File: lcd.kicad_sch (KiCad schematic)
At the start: 6 parts, among them J2 LCD 3.2" 240x320 Conn_01x14_P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

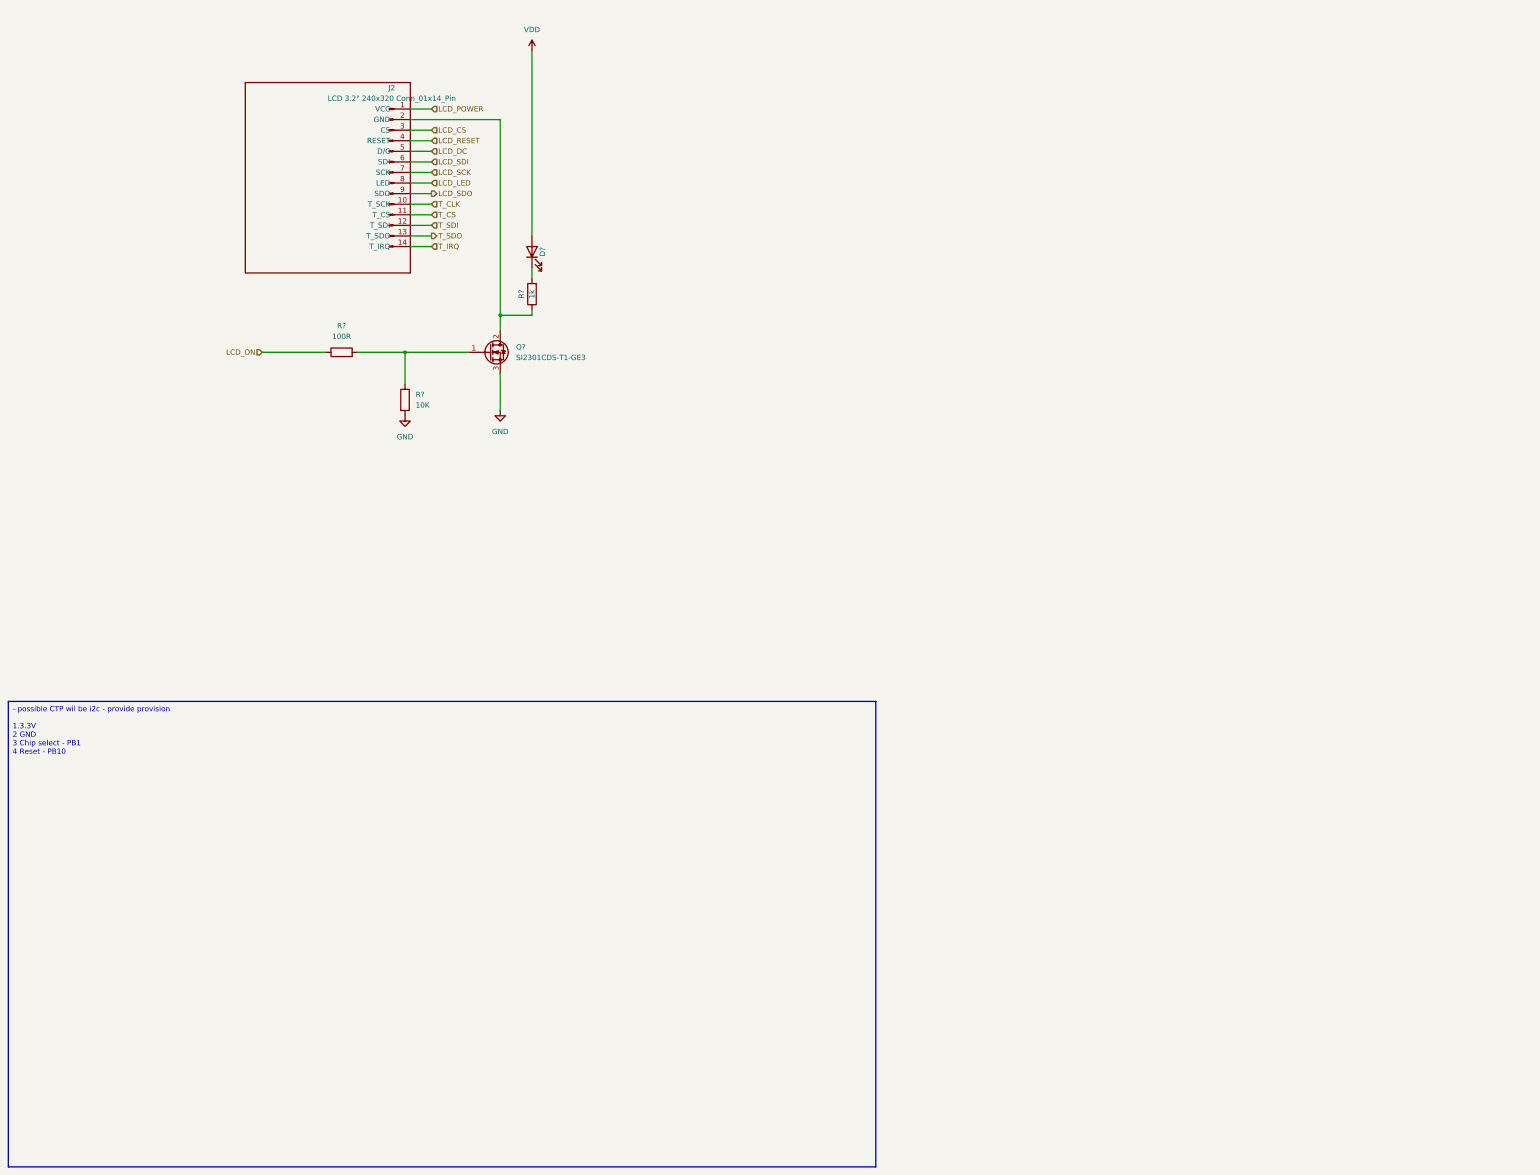
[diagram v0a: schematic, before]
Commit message: change power add buzzer
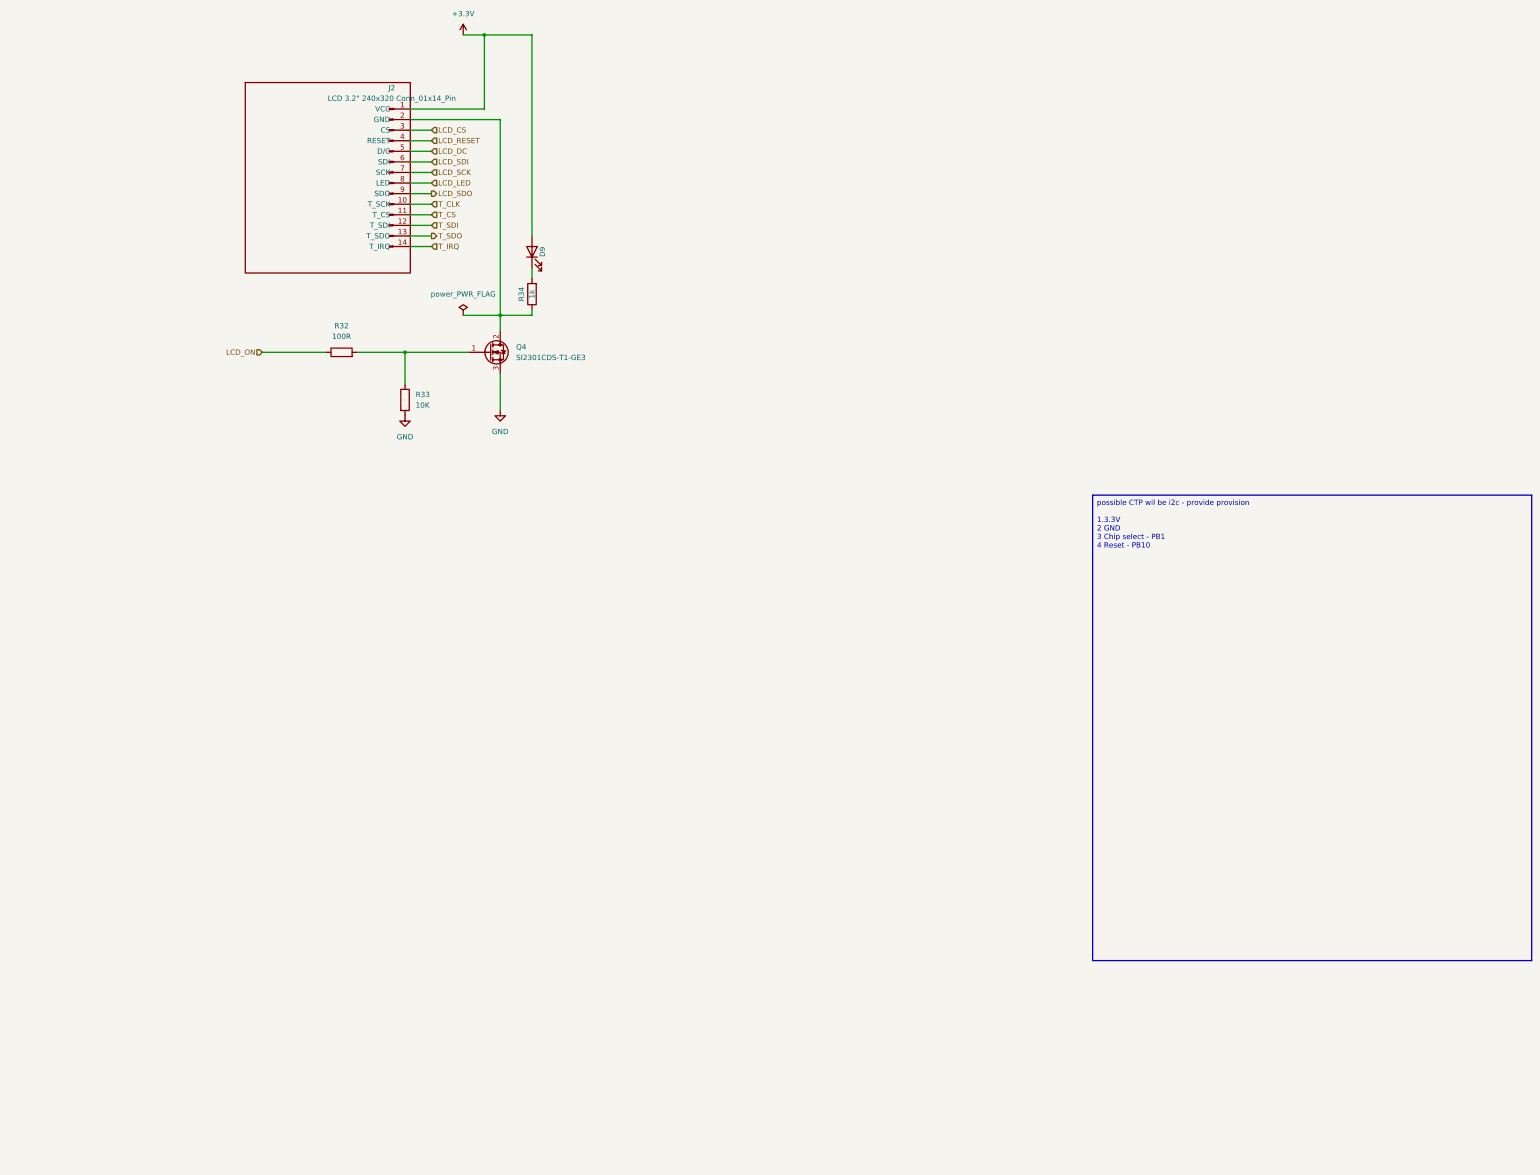
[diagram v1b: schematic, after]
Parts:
- gave numbers to parts that had none: 5
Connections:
- net VDD is gone; now on net +3.3V: D9.2 (A)
- net LCD_POWER renamed +3.3V
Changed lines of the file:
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@@
+	)
+	(junction
+		(at 153.67 27.94)
+		(diameter 0)
+		(color 0 0 0 0)
 	)
 	(junction
@@
 	(wire
 		(pts
-			(xy 135.89 45.72) (xy 140.97 45.72)
+			(xy 135.89 45.72) (xy 153.67 45.72)
 		)
 		(stroke
@@
 	(wire
 		(pts
+			(xy 148.59 95.25) (xy 157.48 95.25)
+		)
+		(stroke
+			(width 0)
+			(type default)
+		)
+	)
+	(wire
+		(pts
 			(xy 123.19 104.14) (xy 134.62 104.14)
 		)
@@
 	(wire
 		(pts
+			(xy 165.1 27.94) (xy 165.1 76.2)
+		)
+		(stroke
+			(width 0)
+			(type default)
+		)
+	)
+	(wire
+		(pts
+			(xy 153.67 27.94) (xy 153.67 45.72)
+		)
+		(stroke
+			(width 0)
+			(type default)
+		)
+	)
+	(wire
+		(pts
 			(xy 135.89 63.5) (xy 140.97 63.5)
 		)
@@
 	(wire
 		(pts
+			(xy 153.67 27.94) (xy 165.1 27.94)
+		)
+		(stroke
+			(width 0)
+			(type default)
+		)
+	)
+	(wire
+		(pts
 			(xy 135.89 53.34) (xy 140.97 53.34)
 		)
@@
 	(wire
 		(pts
+			(xy 148.59 27.94) (xy 153.67 27.94)
+		)
+		(stroke
+			(width 0)
+			(type default)
+		)
+	)
+	(wire
+		(pts
 			(xy 165.1 83.82) (xy 165.1 86.36)
 		)
@@
 	(wire
 		(pts
-			(xy 165.1 31.75) (xy 165.1 76.2)
-		)
-		(stroke
-			(width 0)
-			(type default)
-		)
-	)
-	(wire
-		(pts
 			(xy 100.33 104.14) (xy 115.57 104.14)
 		)
@@
 		)
 	)
-	(text_box "- possible CTP wil be i2c - provide provision\n\n1.3.3V\n2 GND \n3 Chip select - PB1\n4 Reset - PB10\n"
+	(text_box "possible CTP wil be i2c - provide provision\n\n1.3.3V\n2 GND \n3 Chip select - PB1\n4 Reset - PB10\n"
 		(exclude_from_sim no)
-		(at 39.37 187.96 0)
-		(size 208.28 111.76)
+		(at 299.72 138.43 0)
+		(size 105.41 111.76)
 		(stroke
 			(width 0)
@@
 		)
 	)
-	(hierarchical_label "LCD_POWER"
-		(shape input)
-		(at 140.97 45.72 0)
-		(fields_autoplaced yes)
-		(effects
-			(font
-				(size 1.27 1.27)
-			)
-			(justify left)
-		)
-	)
 	(hierarchical_label "LCD_SCK"
 		(shape input)
@@
 			)
 			(justify left)
+		)
+	)
+	(symbol
+		(lib_id "power:+3.3V")
+		(at 148.59 27.94 0)
+		(unit 1)
+		(exclude_from_sim no)
+		(in_bom yes)
+		(on_board yes)
+		(dnp no)
+		(fields_autoplaced yes)
+		(property "Reference" "#PWR034"
+			(at 148.59 31.75 0)
+			(effects
+				(font
+					(size 1.27 1.27)
+				)
+				(hide yes)
+			)
+		)
+		(property "Value" "+3.3V"
+			(at 148.59 22.86 0)
+			(effects
+				(font
+					(size 1.27 1.27)
+				)
+			)
+		)
+		(property "Footprint" ""
+			(at 148.59 27.94 0)
+			(effects
+				(font
+					(size 1.27 1.27)
+				)
+				(hide yes)
+			)
+		)
+		(property "Datasheet" ""
+			(at 148.59 27.94 0)
+			(effects
+				(font
+					(size 1.27 1.27)
+				)
+				(hide yes)
+			)
+		)
+		(property "Description" "Power symbol creates a global label with name \"+3.3V\""
+			(at 148.59 27.94 0)
+			(effects
+				(font
+					(size 1.27 1.27)
+				)
+				(hide yes)
+			)
+		)
+		(pin "1"
+		)
+		(instances
+			(project ""
+				(path "/8d063f79-9282-4820-bcf4-1ff3c006cf08/98bf8f66-79b9-41fc-9cd7-550fbae3319a"
+					(reference "#PWR034")
+					(unit 1)
+				)
+			)
 		)
 	)
@@
 		(on_board yes)
 		(dnp no)
-		(property "Reference" "D?"
+		(property "Reference" "D9"
 			(at 167.64 80.01 0)
 			(effects
@@
 			(project "l8-kicad"
 				(path "/8d063f79-9282-4820-bcf4-1ff3c006cf08/98bf8f66-79b9-41fc-9cd7-550fbae3319a"
-					(reference "D?")
-					(unit 1)
-				)
-			)
-		)
-	)
-	(symbol
-		(lib_id "power:VDD")
-		(at 165.1 31.75 0)
-		(unit 1)
-		(exclude_from_sim no)
-		(in_bom yes)
-		(on_board yes)
-		(dnp no)
-		(fields_autoplaced yes)
-		(property "Reference" "#PWR07"
-			(at 165.1 35.56 0)
-			(effects
-				(font
-					(size 1.27 1.27)
-				)
-				(hide yes)
-			)
-		)
-		(property "Value" "VDD"
-			(at 165.1 26.67 0)
-			(effects
-				(font
-					(size 1.27 1.27)
-				)
-			)
-		)
-		(property "Footprint" ""
-			(at 165.1 31.75 0)
-			(effects
-				(font
-					(size 1.27 1.27)
-				)
-				(hide yes)
-			)
-		)
-		(property "Datasheet" ""
-			(at 165.1 31.75 0)
-			(effects
-				(font
-					(size 1.27 1.27)
-				)
-				(hide yes)
-			)
-		)
-		(property "Description" "Power symbol creates a global label with name \"VDD\""
-			(at 165.1 31.75 0)
-			(effects
-				(font
-					(size 1.27 1.27)
-				)
-				(hide yes)
-			)
-		)
-		(pin "1"
-		)
-		(instances
-			(project ""
-				(path "/8d063f79-9282-4820-bcf4-1ff3c006cf08/98bf8f66-79b9-41fc-9cd7-550fbae3319a"
-					(reference "#PWR07")
+					(reference "D9")
 					(unit 1)
 				)
@@
 		(dnp no)
 		(fields_autoplaced yes)
-		(property "Reference" "R?"
+		(property "Reference" "R32"
 			(at 119.38 97.79 90)
 			(effects
@@
 			(project "l8-kicad"
 				(path "/8d063f79-9282-4820-bcf4-1ff3c006cf08/98bf8f66-79b9-41fc-9cd7-550fbae3319a"
-					(reference "R?")
+					(reference "R32")
+					(unit 1)
+				)
+			)
+		)
+	)
+	(symbol
+		(lib_id "l8-kicad-rescue:PWR_FLAG-power")
+		(at 148.59 95.25 0)
+		(unit 1)
+		(exclude_from_sim no)
+		(in_bom yes)
+		(on_board yes)
+		(dnp no)
+		(fields_autoplaced yes)
+		(property "Reference" "#FLG01"
+			(at 148.59 93.345 0)
+			(effects
+				(font
+					(size 1.27 1.27)
+				)
+				(hide yes)
+			)
+		)
+		(property "Value" "power_PWR_FLAG"
+			(at 148.59 90.17 0)
+			(effects
+				(font
+					(size 1.27 1.27)
+				)
+			)
+		)
+		(property "Footprint" ""
+			(at 148.59 95.25 0)
+			(effects
+				(font
+					(size 1.27 1.27)
+				)
+				(hide yes)
+			)
+		)
+		(property "Datasheet" ""
+			(at 148.59 95.25 0)
+			(effects
+				(font
+					(size 1.27 1.27)
+				)
+				(hide yes)
+			)
+		)
+		(property "Description" ""
+			(at 148.59 95.25 0)
+			(effects
+				(font
+					(size 1.27 1.27)
+				)
+				(hide yes)
+			)
+		)
+		(pin "1"
+		)
+		(instances
+			(project ""
+				(path "/8d063f79-9282-4820-bcf4-1ff3c006cf08/98bf8f66-79b9-41fc-9cd7-550fbae3319a"
+					(reference "#FLG01")
 					(unit 1)
 				)
@@
 		(dnp no)
 		(fields_autoplaced yes)
-		(property "Reference" "Q?"
+		(property "Reference" "Q4"
 			(at 161.29 102.8699 0)
 			(effects
@@
 			(project "l8-kicad"
 				(path "/8d063f79-9282-4820-bcf4-1ff3c006cf08/98bf8f66-79b9-41fc-9cd7-550fbae3319a"
-					(reference "Q?")
+					(reference "Q4")
 					(unit 1)
 				)
@@
 		(on_board yes)
 		(dnp no)
-		(property "Reference" "R?"
+		(property "Reference" "R34"
 			(at 162.56 90.17 90)
 			(effects
@@
 			(project "l8-kicad"
 				(path "/8d063f79-9282-4820-bcf4-1ff3c006cf08/98bf8f66-79b9-41fc-9cd7-550fbae3319a"
-					(reference "R?")
+					(reference "R34")
 					(unit 1)
 				)
@@
 		(dnp no)
 		(fields_autoplaced yes)
-		(property "Reference" "R?"
+		(property "Reference" "R33"
 			(at 137.16 114.2999 0)
 			(effects
@@
 			(project "l8-kicad"
 				(path "/8d063f79-9282-4820-bcf4-1ff3c006cf08/98bf8f66-79b9-41fc-9cd7-550fbae3319a"
-					(reference "R?")
+					(reference "R33")
 					(unit 1)
 				)

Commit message: remove hellen
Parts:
- removed R32: 100R, symbol Device:R
- removed R33: 10K, symbol Device:R
- added R14: 10K, Resistor_SMD:R_0603_1608Metric, symbol Device:R
- added R3: 100R, Resistor_SMD:R_0603_1608Metric, symbol Device:R
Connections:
- net GND: now also R14.1
- net LCD_ON: now also R3.2
- net at Q4.1 (G): now also R14.2, R3.1
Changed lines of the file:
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@@
+	)
+	(symbol
+		(lib_id "Device:R")
+		(at 119.38 104.14 270)
+		(unit 1)
+		(exclude_from_sim no)
+		(in_bom yes)
+		(on_board yes)
+		(dnp no)
+		(property "Reference" "R3"
+			(at 119.38 106.68 90)
+			(effects
+				(font
+					(size 1.27 1.27)
+				)
+			)
+		)
+		(property "Value" "100R"
+			(at 119.38 104.14 90)
+			(effects
+				(font
+					(size 1.27 1.27)
+				)
+			)
+		)
+		(property "Footprint" "Resistor_SMD:R_0603_1608Metric"
+			(at 119.38 102.362 90)
+			(effects
+				(font
+					(size 1.27 1.27)
+				)
+				(hide yes)
+			)
+		)
+		(property "Datasheet" "~"
+			(at 119.38 104.14 0)
+			(effects
+				(font
+					(size 1.27 1.27)
+				)
+				(hide yes)
+			)
+		)
+		(property "Description" "Resistor"
+			(at 119.38 104.14 0)
+			(effects
+				(font
+					(size 1.27 1.27)
+				)
+				(hide yes)
+			)
+		)
+		(property "LCSC" "C21190"
+			(at 119.38 104.14 0)
+			(effects
+				(font
+					(size 1.27 1.27)
+				)
+				(hide yes)
+			)
+		)
+		(property "Manufacturer" "StackPole"
+			(at 119.38 104.14 0)
+			(effects
+				(font
+					(size 1.27 1.27)
+				)
+				(hide yes)
+			)
+		)
+		(property "Part #" "RMCF0603JJ1K00"
+			(at 119.38 104.14 0)
+			(effects
+				(font
+					(size 1.27 1.27)
+				)
+				(hide yes)
+			)
+		)
+		(property "VEND" "DIGI"
+			(at 119.38 104.14 0)
+			(effects
+				(font
+					(size 1.27 1.27)
+				)
+				(hide yes)
+			)
+		)
+		(property "VEND#" "RMCF0603JJ1K00CT-ND"
+			(at 119.38 104.14 0)
+			(effects
+				(font
+					(size 1.27 1.27)
+				)
+				(hide yes)
+			)
+		)
+		(pin "1"
+		)
+		(pin "2"
+		)
+		(instances
+			(project "l8-kicad"
+				(path "/8d063f79-9282-4820-bcf4-1ff3c006cf08/98bf8f66-79b9-41fc-9cd7-550fbae3319a"
+					(reference "R3")
+					(unit 1)
+				)
+			)
+		)
 	)
 	(symbol
@@
 	(symbol
 		(lib_id "Device:R")
-		(at 119.38 104.14 90)
+		(at 134.62 115.57 0)
+		(mirror x)
 		(unit 1)
 		(exclude_from_sim no)
@@
 		(on_board yes)
 		(dnp no)
-		(fields_autoplaced yes)
-		(property "Reference" "R32"
-			(at 119.38 97.79 90)
-			(effects
-				(font
-					(size 1.27 1.27)
-				)
-			)
-		)
-		(property "Value" "100R"
-			(at 119.38 100.33 90)
-			(effects
-				(font
-					(size 1.27 1.27)
-				)
-			)
-		)
-		(property "Footprint" ""
-			(at 119.38 105.918 90)
-			(effects
-				(font
-					(size 1.27 1.27)
+		(property "Reference" "R14"
+			(at 136.652 115.57 90)
+			(effects
+				(font
+					(size 1.27 1.27)
+				)
+			)
+		)
+		(property "Value" "10K"
+			(at 134.62 115.57 90)
+			(effects
+				(font
+					(size 1.27 1.27)
+				)
+			)
+		)
+		(property "Footprint" "Resistor_SMD:R_0603_1608Metric"
+			(at 193.802 173.99 90)
+			(effects
+				(font
+					(size 1.524 1.524)
 				)
 				(hide yes)
@@
 		)
 		(property "Datasheet" "~"
-			(at 119.38 104.14 0)
-			(effects
-				(font
-					(size 1.27 1.27)
+			(at 283.21 174.625 0)
+			(effects
+				(font
+					(size 1.524 1.524)
 				)
 				(hide yes)
@@
 		)
 		(property "Description" "Resistor"
-			(at 119.38 104.14 0)
+			(at 134.62 115.57 0)
+			(effects
+				(font
+					(size 1.27 1.27)
+				)
+				(hide yes)
+			)
+		)
+		(property "Part #" "RMCF0603JT10K0"
+			(at 16.51 8.89 0)
+			(effects
+				(font
+					(size 1.27 1.27)
+				)
+				(hide yes)
+			)
+		)
+		(property "VEND" "DIGI"
+			(at 16.51 8.89 0)
+			(effects
+				(font
+					(size 1.27 1.27)
+				)
+				(hide yes)
+			)
+		)
+		(property "VEND#" "RMCF0603JT10K0CT-ND"
+			(at 16.51 8.89 0)
+			(effects
+				(font
+					(size 1.27 1.27)
+				)
+				(hide yes)
+			)
+		)
+		(property "Manufacturer" "StackPole"
+			(at 16.51 8.89 0)
+			(effects
+				(font
+					(size 1.27 1.27)
+				)
+				(hide yes)
+			)
+		)
+		(property "LCSC" "C25804"
+			(at 134.62 115.57 0)
 			(effects
 				(font
@@
 			(project "l8-kicad"
 				(path "/8d063f79-9282-4820-bcf4-1ff3c006cf08/98bf8f66-79b9-41fc-9cd7-550fbae3319a"
-					(reference "R32")
+					(reference "R14")
 					(unit 1)
 				)
@@
 					(unit 1)
 				)
-			)
-		)
-	)
-	(symbol
-		(lib_id "Device:R")
-		(at 134.62 115.57 0)
-		(unit 1)
-		(exclude_from_sim no)
-		(in_bom yes)
-		(on_board yes)
-		(dnp no)
-		(fields_autoplaced yes)
-		(property "Reference" "R33"
-			(at 137.16 114.2999 0)
-			(effects
-				(font
-					(size 1.27 1.27)
-				)
-				(justify left)
-			)
-		)
-		(property "Value" "10K"
-			(at 137.16 116.8399 0)
-			(effects
-				(font
-					(size 1.27 1.27)
-				)
-				(justify left)
-			)
-		)
-		(property "Footprint" ""
-			(at 132.842 115.57 90)
-			(effects
-				(font
-					(size 1.27 1.27)
-				)
-				(hide yes)
-			)
-		)
-		(property "Datasheet" "~"
-			(at 134.62 115.57 0)
-			(effects
-				(font
-					(size 1.27 1.27)
-				)
-				(hide yes)
-			)
-		)
-		(property "Description" "Resistor"
-			(at 134.62 115.57 0)
-			(effects
-				(font
-					(size 1.27 1.27)
-				)
-				(hide yes)
-			)
-		)
-		(pin "1"
-		)
-		(pin "2"
-		)
-		(instances
-			(project "l8-kicad"
-				(path "/8d063f79-9282-4820-bcf4-1ff3c006cf08/98bf8f66-79b9-41fc-9cd7-550fbae3319a"
-					(reference "R33")
-					(unit 1)
-				)

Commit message: pre quilter
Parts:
- added R37, R38, R39: 10K, Resistor_SMD:R_0603_1608Metric, symbol Device:R
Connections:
- net +3.3V: now also R37.2, R38.2, R39.2
- net LCD_CS: now also R37.1
- net LCD_RESET: now also R38.1
- net T_CS: now also R39.1
